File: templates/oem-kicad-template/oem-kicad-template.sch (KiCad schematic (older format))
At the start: 26 parts

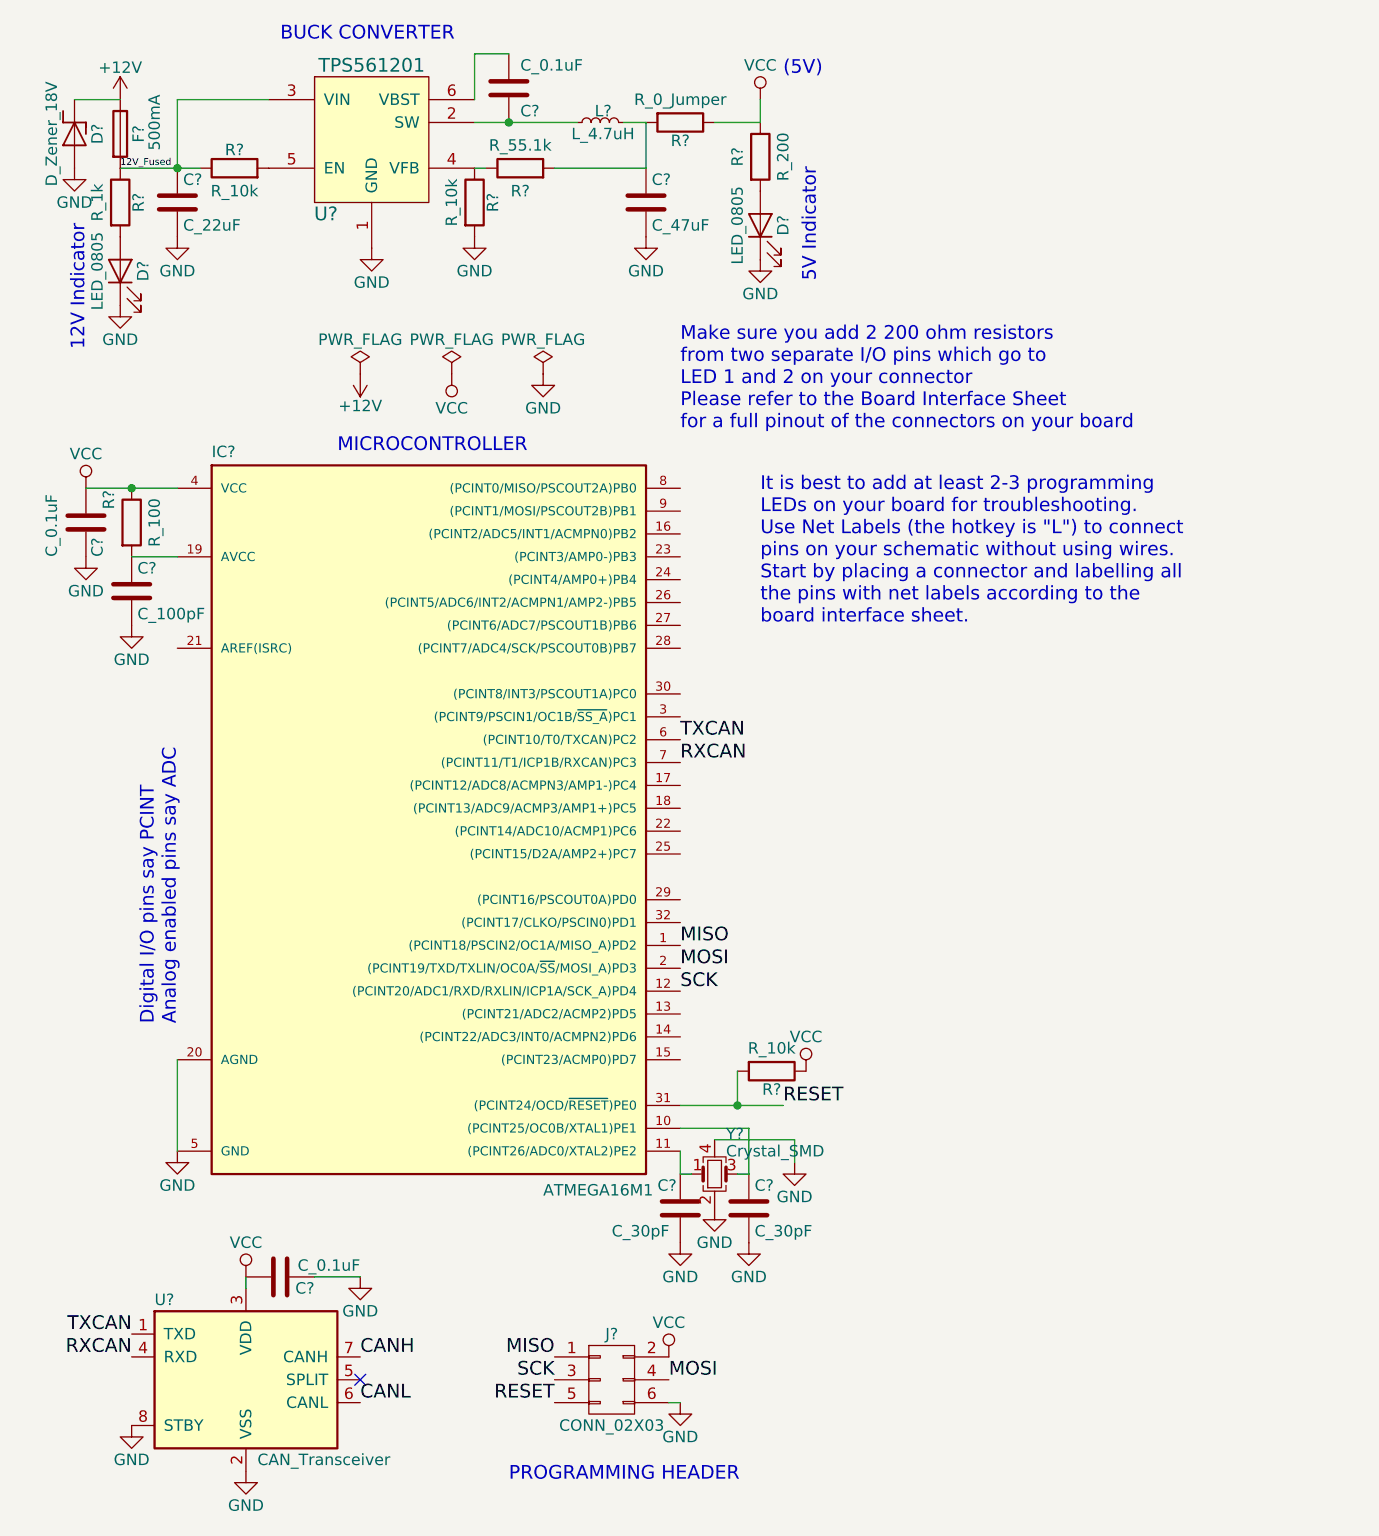
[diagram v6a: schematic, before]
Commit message: fixed some issues with template schematic
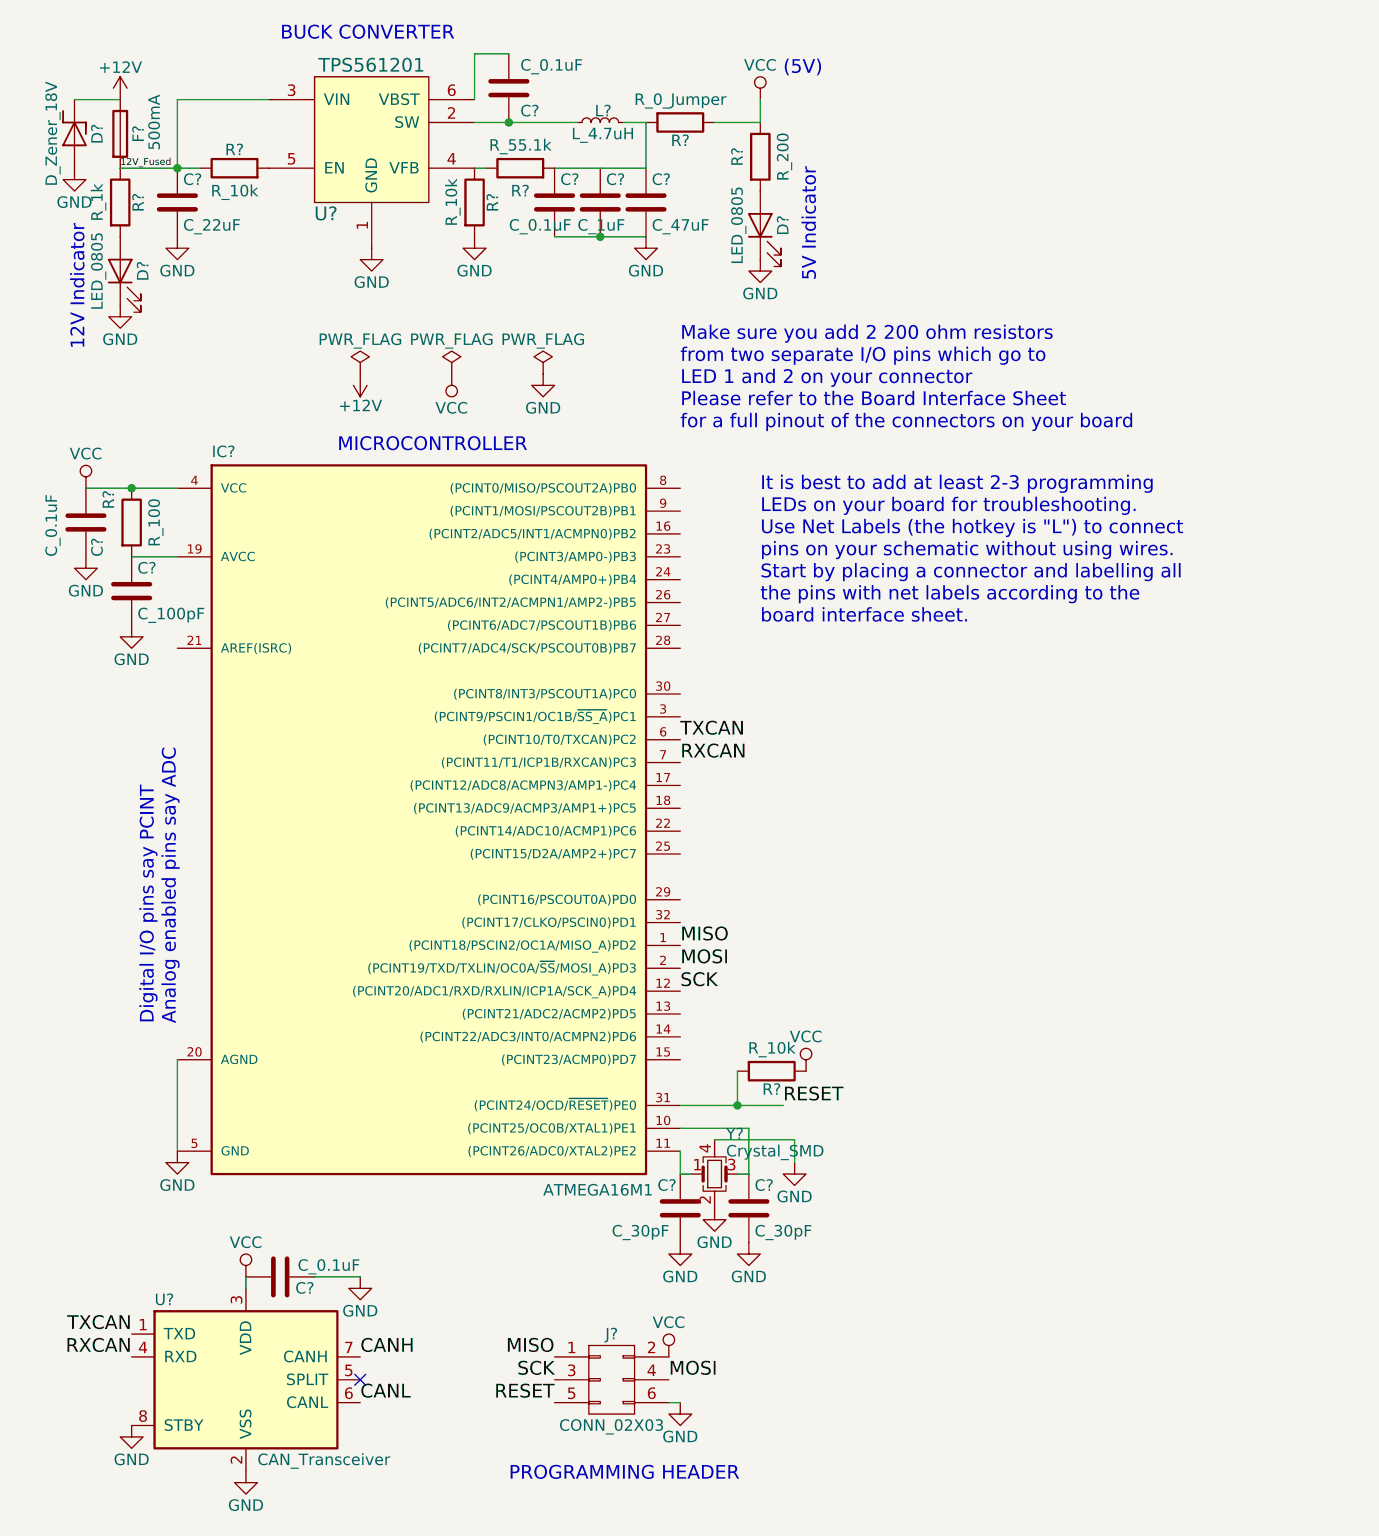
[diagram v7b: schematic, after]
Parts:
- added C?: C_1uF, footprints:C_0805_OEM, symbol C_1uF
- added C?: C_0.1uF, footprints:C_0805_OEM, symbol C_0.1uF
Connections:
- net GND: now also C?.2, C?.2
- net at C?.1, L?.2, R?.2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: now also C?.1
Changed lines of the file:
@@
 $EndComp
 Wire Wire Line
-	2500 950  2650 950
-Wire Wire Line
-	2650 950  2950 950
+	2500 950  2950 950
 Wire Wire Line
 	2500 850  2500 650
@@
 $EndComp
 Wire Wire Line
-	800  2550 1000 2550
-Wire Wire Line
-	1000 2550 1200 2550
+	800  2550 1200 2550
 Connection ~ 1000 2550
 Wire Wire Line
-	950  1150 1200 1150
-Wire Wire Line
-	1200 1150 1300 1150
+	950  1150 1300 1150
 Connection ~ 1200 1150
 Wire Wire Line
-	3400 5250 3650 5250
-Wire Wire Line
-	3650 5250 3850 5250
+	3400 5250 3850 5250
 Wire Wire Line
 	3650 5100 3650 5250
@@
 Wire Wire Line
 	750  850  950  850
+$Comp
+L C_1uF C?
+U 1 1 5A8235EB
+P 3050 1300
+F 0 "C?" H 3075 1400 50  0000 L CNN
+F 1 "C_1uF" H 2950 1200 50  0000 L CNN
+F 2 "footprints:C_0805_OEM" H 3088 1150 50  0001 C CNN
+F 3 "http://datasheets.avx.com/X7RDielectric.pdf" H 3075 1400 50  0001 C CNN
+F 4 "CAP CER 1UF 25V X7R 0805" H 3575 1900 60  0001 C CNN "Description"
+F 5 "478-10487-1-ND" H 3050 1300 60  0001 C CNN "MPN"
+F 6 "Digi-Key" H 3050 1300 60  0001 C CNN "MFN"
+F 7 "Value" H 3050 1300 60  0001 C CNN "Package"
+F 8 "https://www.digikey.com/product-detail/en/avx-corporation/08053C105JAT2A/478-10487-1-ND/6797628" H 3475 1800 60  0001 C CNN "PurchasingLink"
+	1    3050 1300
+	1    0    0    -1
+$EndComp
+$Comp
+L C_0.1uF C?
+U 1 1 5A82366B
+P 2850 1300
+F 0 "C?" H 2875 1400 50  0000 L CNN
+F 1 "C_0.1uF" H 2650 1200 50  0000 L CNN
+F 2 "footprints:C_0805_OEM" H 2888 1150 50  0001 C CNN
+F 3 "http://datasheets.avx.com/X7RDielectric.pdf" H 2875 1400 50  0001 C CNN
+F 4 "478-3352-1-ND" H 2850 1300 60  0001 C CNN "MPN"
+F 5 "Digi-Key" H 2850 1300 60  0001 C CNN "MFN"
+F 6 "Value" H 2850 1300 60  0001 C CNN "Package"
+F 7 "https://www.digikey.com/products/en?keywords=478-3352-1-ND" H 3275 1800 60  0001 C CNN "PurchasingLink"
+	1    2850 1300
+	1    0    0    -1
+$EndComp
+Wire Wire Line
+	2850 1450 3250 1450
+Connection ~ 3050 1450
 $EndSCHEMATC
